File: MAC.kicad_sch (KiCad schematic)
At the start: 16 parts, among them J10 Conn_01x30_Male, SW1 RotaryEncoder_Switch

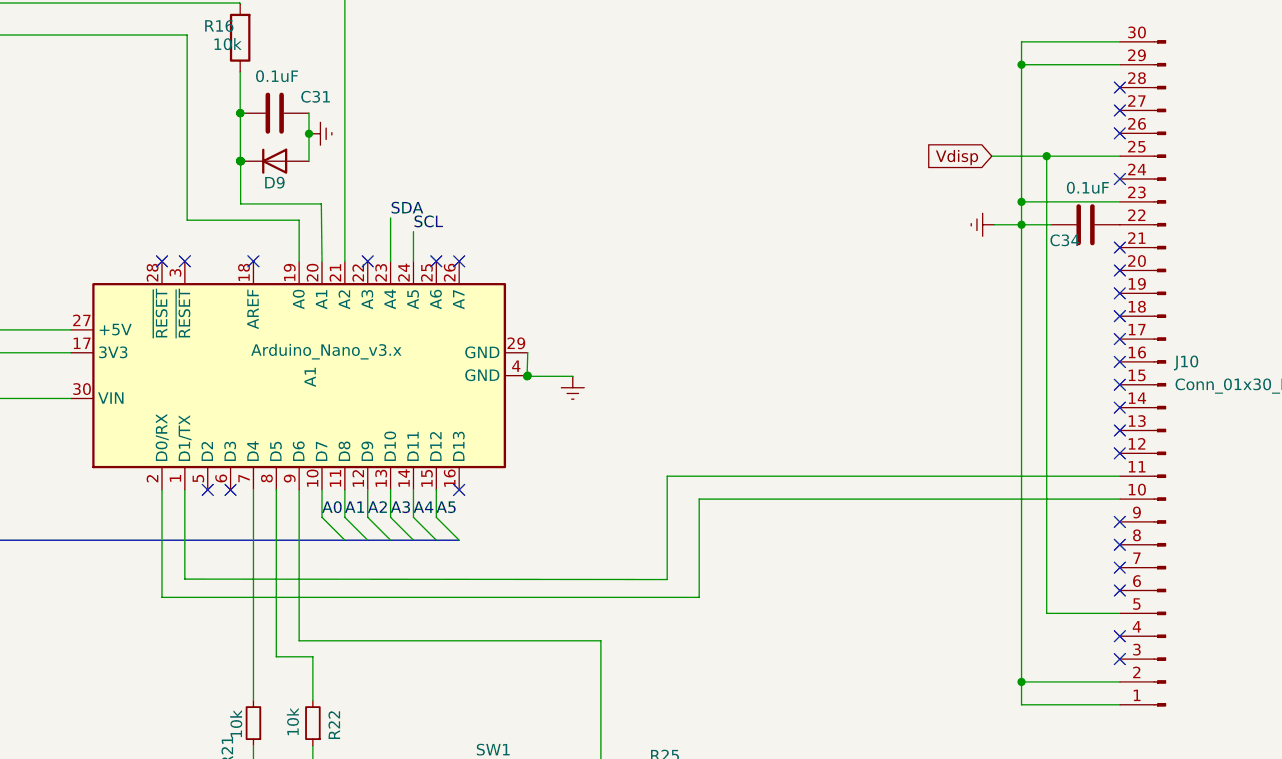
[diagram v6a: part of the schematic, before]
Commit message: repositioned signal wires and started mapping OLED and rotary encoder
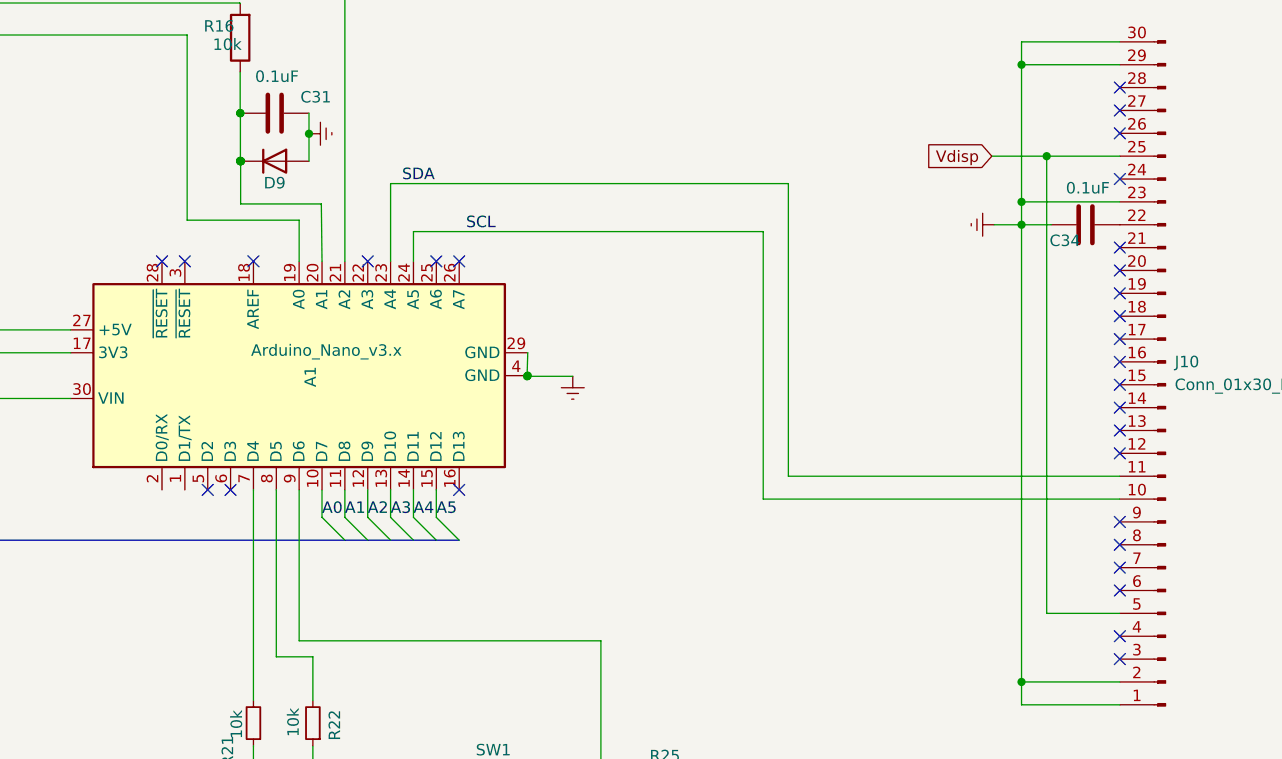
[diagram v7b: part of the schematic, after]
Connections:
- net SCL: now also J10.10 (Pin_10)
- net SDA: now also J10.11 (Pin_11)
- net at A1.2 (D0/RX): no longer J10.10 (Pin_10)
- net at A1.1 (D1/TX): no longer J10.11 (Pin_11)
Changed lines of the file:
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@@
+    (stroke (width 0) (type default) (color 0 0 0 0))
+  )
+  (wire (pts (xy 175.514 79.248) (xy 175.514 46.736))
     (stroke (width 0) (type default) (color 0 0 0 0))
   )
@@
     (stroke (width 0) (type default) (color 0 0 0 0))
   )
-  (wire (pts (xy 105.918 80.772) (xy 105.918 92.71))
-    (stroke (width 0) (type default) (color 0 0 0 0))
-  )
   (wire (pts (xy 114.6048 34.3408) (xy 114.6048 38.9128))
     (stroke (width 0) (type default) (color 0 0 0 0))
@@
     (stroke (width 0) (type default) (color 0 0 0 0))
   )
-  (wire (pts (xy 165.608 81.788) (xy 212.344 81.788))
+  (wire (pts (xy 172.72 81.788) (xy 212.344 81.788))
     (stroke (width 0) (type default) (color 0 0 0 0))
   )
@@
     (stroke (width 0) (type default) (color 0 0 0 0))
   )
-  (wire (pts (xy 162.052 90.7288) (xy 108.458 90.678))
-    (stroke (width 0) (type default) (color 0 0 0 0))
-  )
   (wire (pts (xy 212.344 48.768) (xy 201.422 48.768))
     (stroke (width 0) (type default) (color 0 0 0 0))
@@
     (stroke (width 0) (type default) (color 0 0 0 0))
   )
-  (wire (pts (xy 212.344 79.248) (xy 162.052 79.248))
+  (wire (pts (xy 212.344 79.248) (xy 175.514 79.248))
     (stroke (width 0) (type default) (color 0 0 0 0))
   )
@@
     (stroke (width 0) (type default) (color 0 0 0 0))
   )
+  (wire (pts (xy 172.72 52.07) (xy 172.72 81.788))
+    (stroke (width 0) (type default) (color 0 0 0 0))
+  )
   (wire (pts (xy 113.03 116.84) (xy 116.078 116.84))
     (stroke (width 0) (type default) (color 0 0 0 0))
   )
+  (wire (pts (xy 133.858 52.07) (xy 172.72 52.07))
+    (stroke (width 0) (type default) (color 0 0 0 0))
+  )
   (wire (pts (xy 114.6556 44.2468) (xy 114.6556 48.9966))
     (stroke (width 0) (type default) (color 0 0 0 0))
@@
     (stroke (width 0) (type default) (color 0 0 0 0))
   )
-  (wire (pts (xy 105.918 92.71) (xy 165.608 92.71))
+  (wire (pts (xy 175.514 46.736) (xy 131.318 46.736))
     (stroke (width 0) (type default) (color 0 0 0 0))
   )
@@
     (stroke (width 0) (type default) (color 0 0 0 0))
   )
-  (wire (pts (xy 108.458 90.678) (xy 108.458 80.772))
-    (stroke (width 0) (type default) (color 0 0 0 0))
-  )
   (wire (pts (xy 201.422 33.528) (xy 201.422 48.768))
     (stroke (width 0) (type default) (color 0 0 0 0))
@@
     (stroke (width 0) (type default) (color 0 0 0 0))
   )
-  (wire (pts (xy 162.052 79.248) (xy 162.052 90.7288))
-    (stroke (width 0) (type default) (color 0 0 0 0))
-  )
   (bus (pts (xy 55.626 86.36) (xy 126.238 86.36))
     (stroke (width 0) (type default) (color 0 0 0 0))
@@
     (stroke (width 0) (type default) (color 0 0 0 0))
   )
-  (wire (pts (xy 165.608 92.71) (xy 165.608 81.788))
-    (stroke (width 0) (type default) (color 0 0 0 0))
-  )
   (wire (pts (xy 114.6556 44.2468) (xy 114.7064 44.2468))
     (stroke (width 0) (type default) (color 0 0 0 0))
@@
     (stroke (width 0) (type default) (color 0 0 0 0))
   )
-  (wire (pts (xy 131.318 55.372) (xy 131.318 50.546))
+  (wire (pts (xy 131.318 46.736) (xy 131.318 55.372))
     (stroke (width 0) (type default) (color 0 0 0 0))
   )
@@
     (effects (font (size 1.27 1.27)) (justify left bottom))
   )
-  (label "SDA" (at 131.318 50.546 0)
+  (label "SDA" (at 132.588 46.736 0)
     (effects (font (size 1.27 1.27)) (justify left bottom))
   )
@@
     (effects (font (size 1.27 1.27)) (justify left bottom))
   )
-  (label "SCL" (at 133.858 52.07 0)
-    (effects (font (size 1.27 1.27)) (justify left bottom))
-  )
+  (label "SCL" (at 139.7 52.07 0)
+    (effects (font (size 1.27 1.27)) (justify left bottom))
+  )

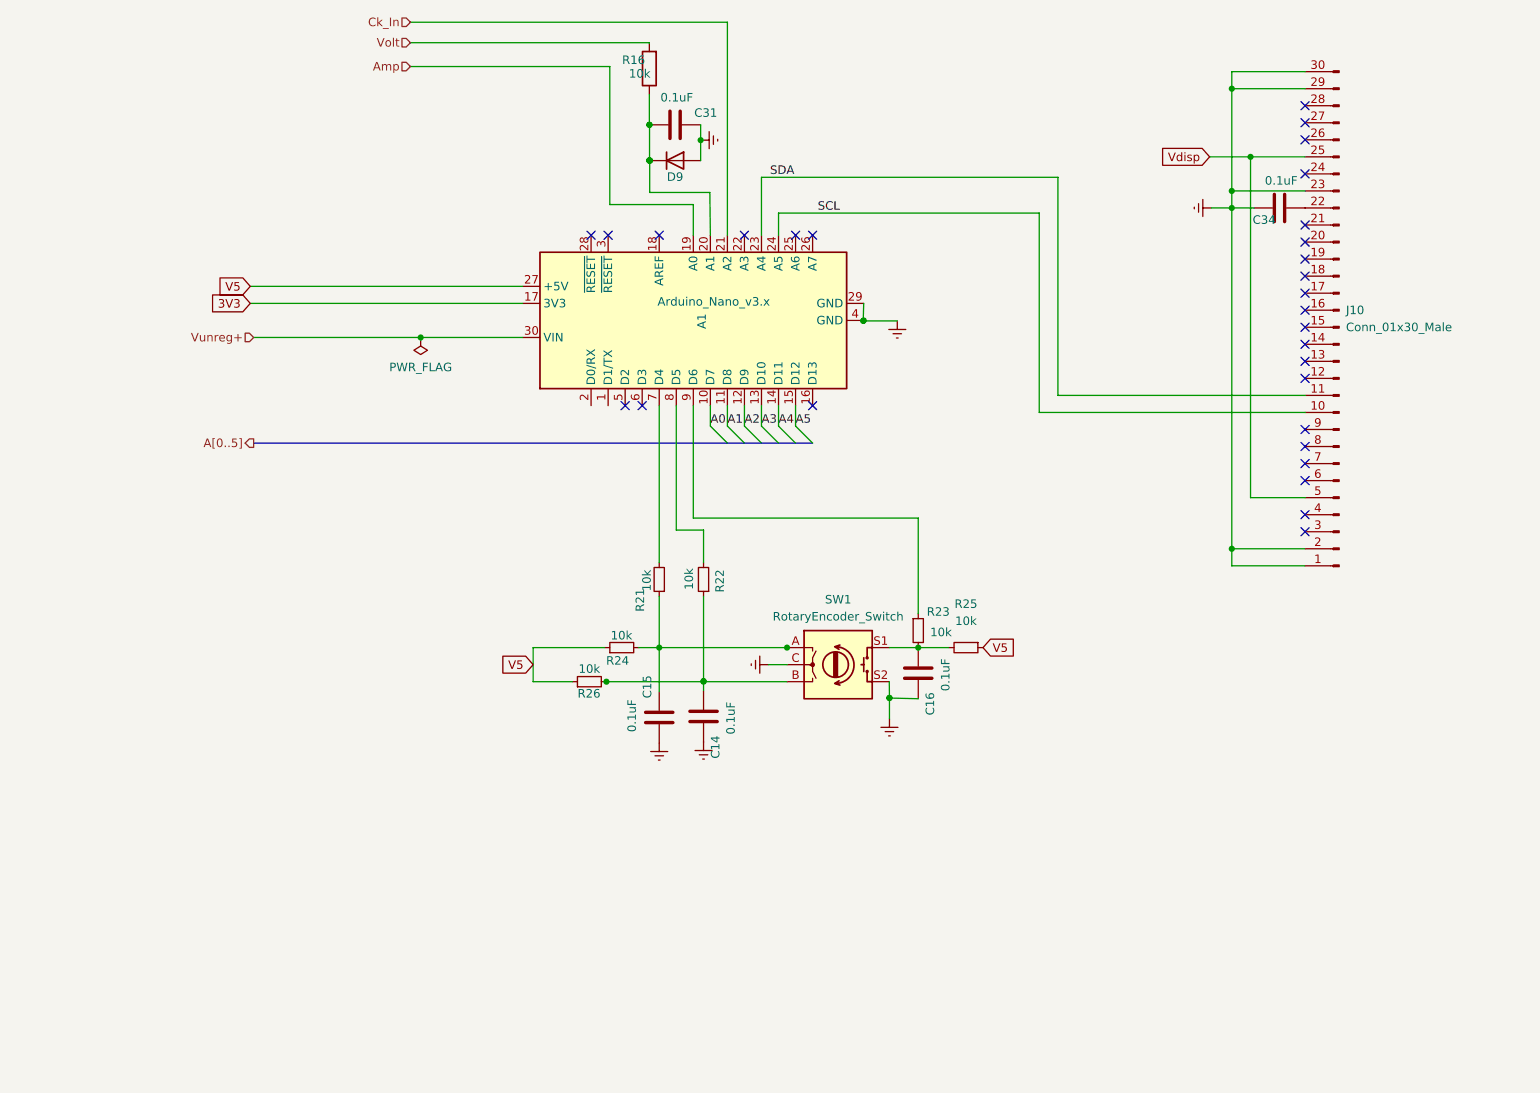
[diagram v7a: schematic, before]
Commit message: adding diff and summing amps to scale amp inputs
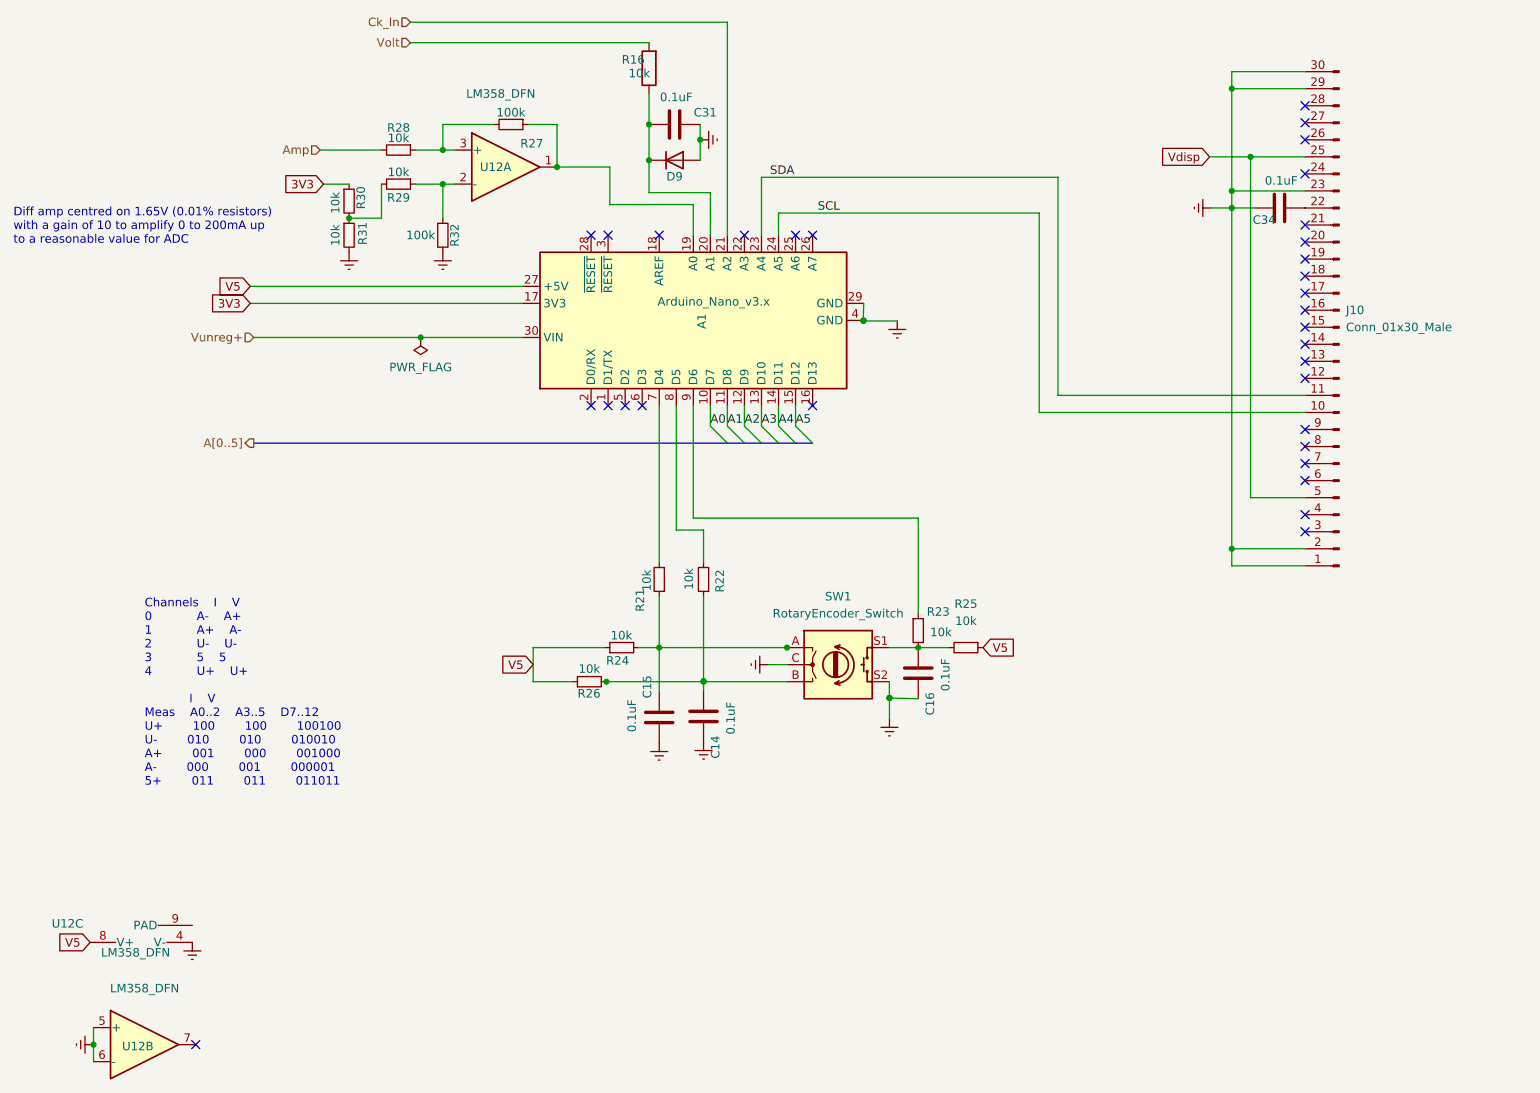
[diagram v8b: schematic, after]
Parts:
- added R27, R32: 100k, Resistor_SMD:R_0603_1608Metric, symbol Device:R_Small
- added R28, R29, R30, R31: 10k, Resistor_SMD:R_0603_1608Metric, symbol Device:R_Small
- added U12: LM358_DFN, Package_DFN_QFN:DFN-8-1EP_2x2mm_P0.5mm_EP1.05x1.75mm, symbol Amplifier_Operational:LM358_DFN
- SW1: footprint Rotary_Encoder:RotaryEncoder_Alps_EC11E_Vertical_H20mm -> Rotary_Encoder:RotaryEncoder_Alps_EC11E-Switch_Vertical_H20mm_CircularMountingHoles
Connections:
- net 3V3: now also R30.1
- net Amp: now also R28.2; no longer A1.19 (A0)
- net GNDREF: now also R31.2, R32.2, U12.4 (V-), U12.5 (+), U12.6 (-)
- net V5: now also U12.8 (V+)
- new net: R29.1, R32.1, U12.2 (-)
- new net: R29.2, R30.2, R31.1
- new net: R27.2, R28.1, U12.3 (+)
- new net: A1.19 (A0), R27.1, U12.1
- no-connect marks 29 -> 32
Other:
- note added: "Channels I V 0 A- A+ 1 A+ A- 2 U- U- 3 5 5 4 U+ U+ I V Meas A0..2 A3..5 D7..12 U+ 100 100 100100 U- 010 010 010010 A+ 001 000 001000 A- 000 001 000001 5+ 011 011 011011"
- note added: "Diff amp centred on 1.65V (0.01% resistors) with a gain of 10 to amplify 0 to 200mA up to a reasonable value for ADC"
